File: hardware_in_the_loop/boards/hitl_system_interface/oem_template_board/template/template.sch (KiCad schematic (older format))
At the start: 39 parts, among them J1 CONN_02X03, U1 MCP2561-E_SN, U101 TPS560430YF, U2 ATMEGA16M1, Y1 Crystal_SMD

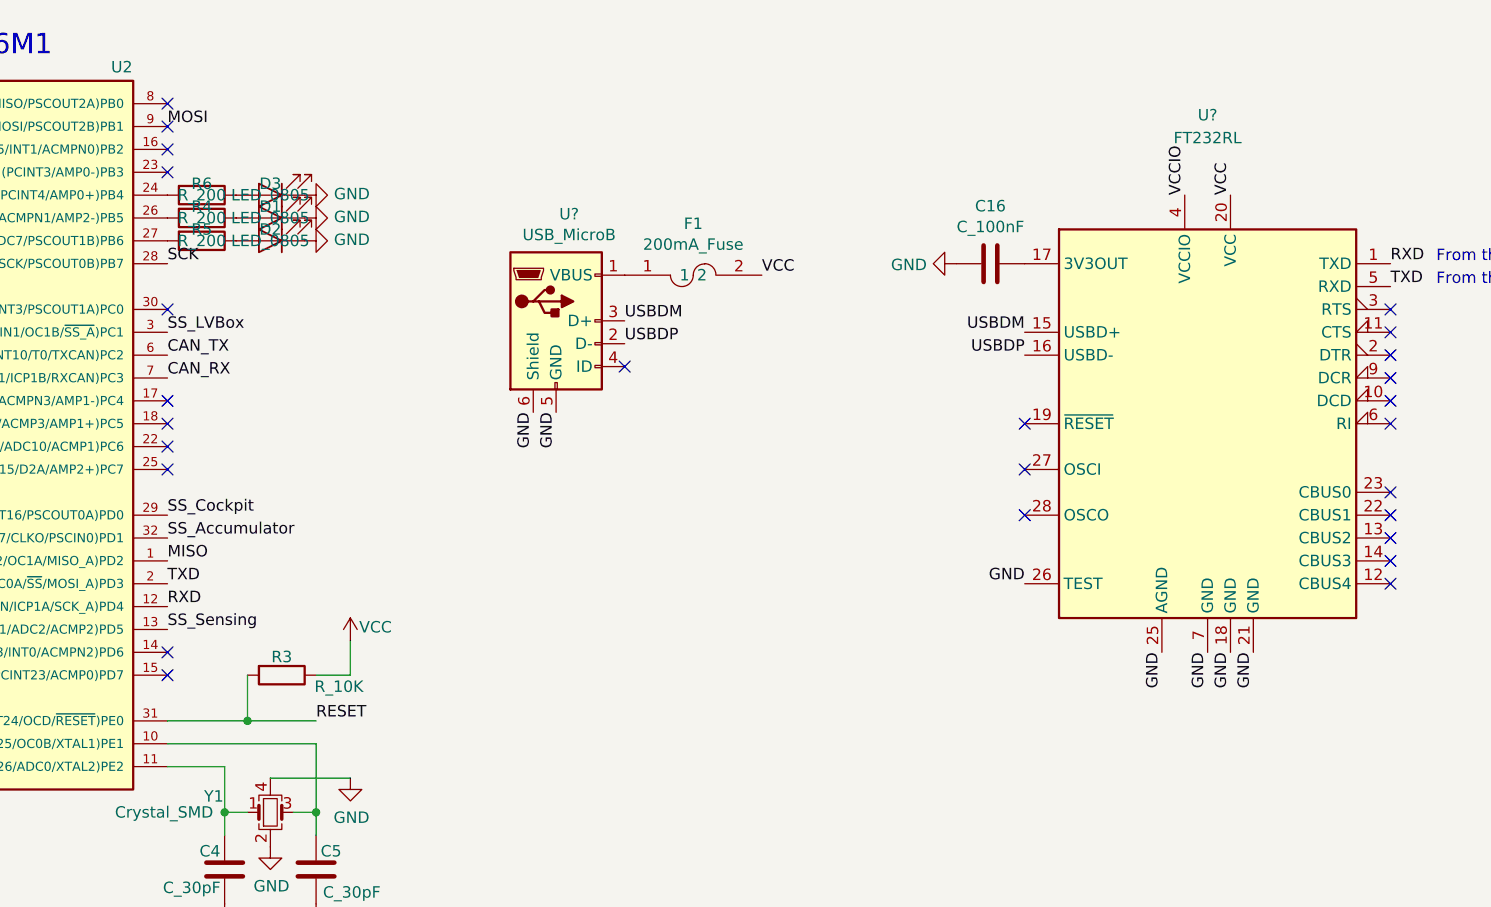
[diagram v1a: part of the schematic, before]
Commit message: Changed GND and VCC pins to power flags, added Nanofit8 connector, modified USBDP and USBDM connections on USB_Micro and FT232RL
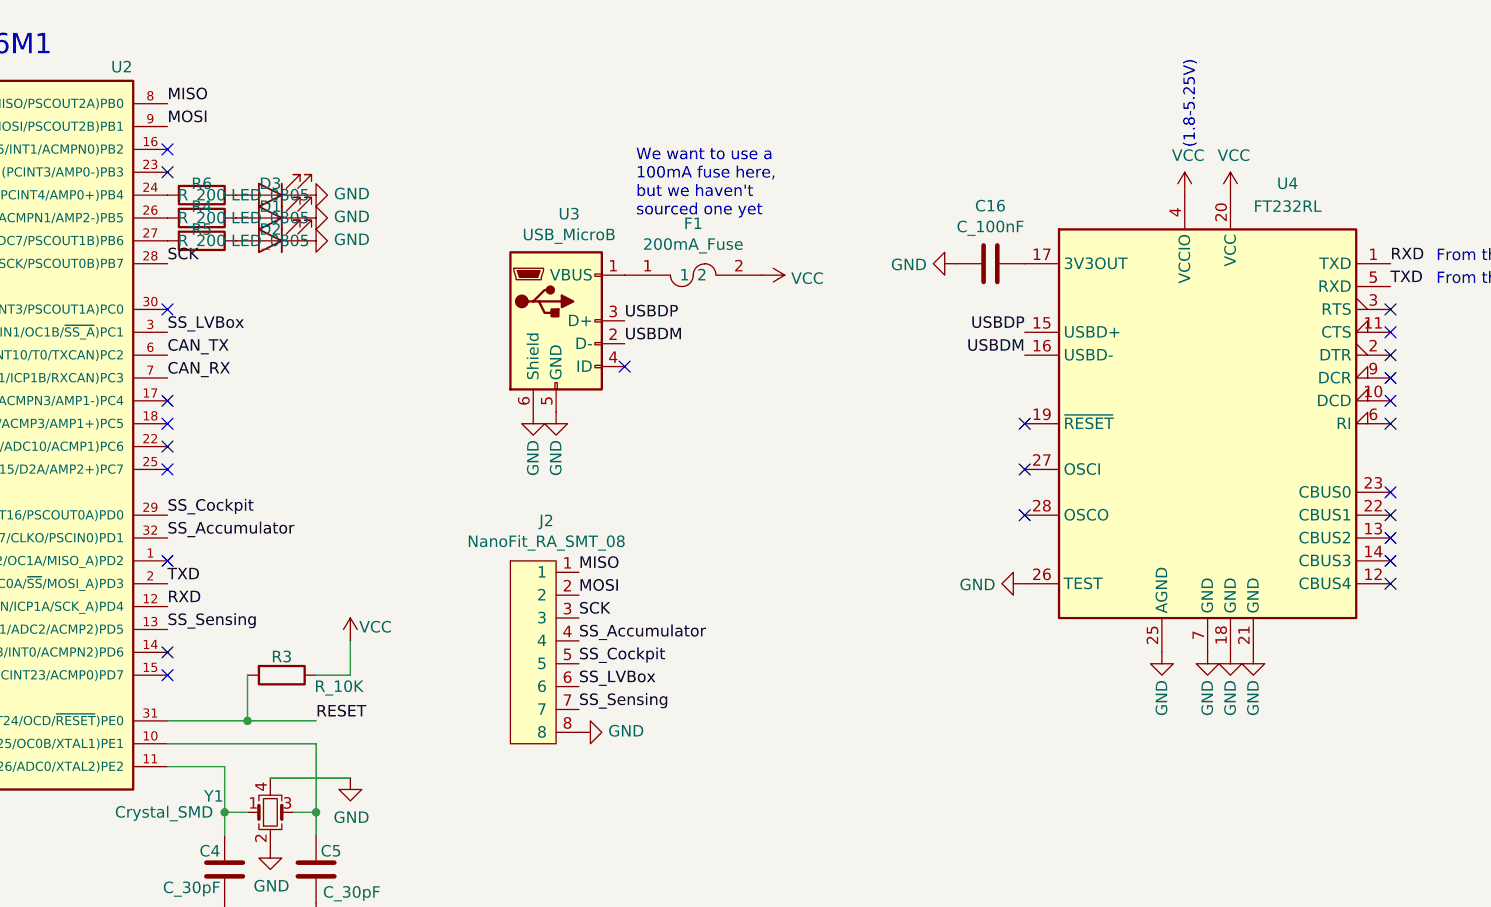
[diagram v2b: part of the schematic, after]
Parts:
- added J2: NanoFit_RA_SMT_08, footprints:NanoFit_RA_8, symbol formula:NanoFit_RA_SMT_08
- gave numbers to parts that had none: 2
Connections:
- net VCCIO is gone; now on net VCC: U4.4 (VCCIO)
- net GND: now also J2.8
- net MISO: now also U2.8 ((PCINT0/MISO/PSCOUT2A)PB0), J2.1; no longer U2.1 ((PCINT18/PSCIN2/OC1A/MISO_A)PD2)
- net MOSI: now also J2.2
- net SCK: now also J2.3
- net SS_Accumulator: now also J2.4
- net SS_Cockpit: now also J2.5
- net SS_LVBox: now also J2.6
- net SS_Sensing: now also J2.7
- net USBDM: now also U3.2 (D-), U4.16 (USBD-); no longer U3.3 (D+), U4.15 (USBD+)
- net USBDP: now also U3.3 (D+), U4.15 (USBD+); no longer U3.2 (D-), U4.16 (USBD-)
- no-connect marks 28 -> 27
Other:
- note added: "(1.8-5.25V)"
- note added: "We want to use a \n100mA fuse here, \nbut we haven't \nsourced one yet\n"
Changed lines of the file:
@@
 Text Label 3650 2200 0    50   ~ 0
 CAN_RX
-Text Label 3650 3000 0    50   ~ 0
-MISO
 Text Label 3650 1100 0    50   ~ 0
 MOSI
@@
 	0    -1   -1   0
 $EndComp
-NoConn ~ 3650 1000
-NoConn ~ 3650 1100
 NoConn ~ 3650 1200
 NoConn ~ 3650 1300
@@
 NoConn ~ 9000 1900
 NoConn ~ 9000 2000
-Text Label 8000 3400 3    50   ~ 0
-GND
-Text Label 8200 3400 3    50   ~ 0
-GND
-Text Label 8300 3400 3    50   ~ 0
-GND
-Text Label 8400 3400 3    50   ~ 0
-GND
-Text Label 7400 3100 2    50   ~ 0
-GND
 NoConn ~ 9000 2700
 NoConn ~ 9000 2800
@@
 $EndComp
 $Comp
-L power:GND #PWR?
+L power:GND #PWR028
 U 1 1 5FA19E14
 P 7100 1700
-F 0 "#PWR?" H 7100 1450 50  0001 C CNN
+F 0 "#PWR028" H 7100 1450 50  0001 C CNN
 F 1 "GND" V 7105 1572 50  0000 R CNN
 F 2 "" H 7100 1700 50  0001 C CNN
@@
 $EndComp
 $Comp
-L formula:USB_MicroB U?
+L formula:USB_MicroB U3
 U 1 1 5FA24431
 P 5350 1950
-F 0 "U?" H 5407 2417 50  0000 C CNN
+F 0 "U3" H 5407 2417 50  0000 C CNN
 F 1 "USB_MicroB" H 5407 2326 50  0000 C CNN
 F 2 "Connectors_USB:USB_Micro-B_Molex-105017-0001" H 5300 2300 50  0001 C CNN
@@
 	1    0    0    -1
 $EndComp
-Text Label 5350 2350 3    50   ~ 0
-GND
-Text Label 5250 2350 3    50   ~ 0
-GND
 NoConn ~ 5650 2150
 $Comp
-L formula:FT232RL U?
+L formula:FT232RL U4
 U 1 1 5F9FAF59
 P 8200 2400
-F 0 "U?" H 8200 3750 50  0000 C CNN
-F 1 "FT232RL" H 8200 3650 50  0000 C CNN
+F 0 "U4" H 8550 3450 50  0000 C CNN
+F 1 "FT232RL" H 8550 3350 50  0000 C CNN
 F 2 "Package_SO:SSOP-28_5.3x10.2mm_P0.65mm" H 9300 1500 50  0001 C CNN
 F 3 "https://www.ftdichip.com/Support/Documents/DataSheets/ICs/DS_FT232R.pdf" H 8200 2400 50  0001 C CNN
@@
 	1    0    0    -1
 $EndComp
-Text Label 8300 1400 1    50   ~ 0
-VCC
 Text Label 7400 2000 2    50   ~ 0
+USBDP
+Text Label 7400 2100 2    50   ~ 0
 USBDM
-Text Label 7400 2100 2    50   ~ 0
+Text Label 5650 1950 0    50   ~ 0
 USBDP
-Text Label 8100 1400 1    50   ~ 0
-VCCIO
-Text Label 5650 1950 0    50   ~ 0
+Text Label 5650 2050 0    50   ~ 0
 USBDM
-Text Label 5650 2050 0    50   ~ 0
-USBDP
 NoConn ~ 7400 2400
 NoConn ~ 7400 2600
@@
 	1    0    0    -1
 $EndComp
-Text Label 6250 1750 0    50   ~ 0
-VCC
+Text Label 3650 1000 0    50   ~ 0
+MISO
+NoConn ~ 3650 3000
+Text Notes 5700 1500 0    50   ~ 0
+We want to use a \n100mA fuse here, \nbut we haven't \nsourced one yet\n
+$Comp
+L power:GND #PWR025
+U 1 1 5FA26E89
+P 5350 2350
+F 0 "#PWR025" H 5350 2100 50  0001 C CNN
+F 1 "GND" V 5350 2150 50  0000 C CNN
+F 2 "" H 5350 2350 50  0001 C CNN
+F 3 "" H 5350 2350 50  0001 C CNN
+	1    5350 2350
+	1    0    0    -1
+$EndComp
+$Comp
+L power:GND #PWR024
+U 1 1 5FA2D38B
+P 5250 2350
+F 0 "#PWR024" H 5250 2100 50  0001 C CNN
+F 1 "GND" V 5250 2150 50  0000 C CNN
+F 2 "" H 5250 2350 50  0001 C CNN
+F 3 "" H 5250 2350 50  0001 C CNN
+	1    5250 2350
+	1    0    0    -1
+$EndComp
+$Comp
+L power:VCC #PWR027
+U 1 1 5FA2F0E9
+P 6250 1750
+F 0 "#PWR027" H 6250 1600 50  0001 C CNN
+F 1 "VCC" V 6265 1878 50  0000 L CNN
+F 2 "" H 6250 1750 50  0001 C CNN
+F 3 "" H 6250 1750 50  0001 C CNN
+	1    6250 1750
+	0    1    1    0
+$EndComp
+$Comp
+L power:VCC #PWR033
+U 1 1 5FA315C6
+P 8300 1400
+F 0 "#PWR033" H 8300 1250 50  0001 C CNN
+F 1 "VCC" H 8315 1573 50  0000 C CNN
+F 2 "" H 8300 1400 50  0001 C CNN
+F 3 "" H 8300 1400 50  0001 C CNN
+	1    8300 1400
+	1    0    0    -1
+$EndComp
+$Comp
+L power:VCC #PWR031
+U 1 1 5FA321E6
+P 8100 1400
+F 0 "#PWR031" H 8100 1250 50  0001 C CNN
+F 1 "VCC" H 8115 1573 50  0000 C CNN
+F 2 "" H 8100 1400 50  0001 C CNN
+F 3 "" H 8100 1400 50  0001 C CNN
+	1    8100 1400
+	1    0    0    -1
+$EndComp
+Text Notes 8150 1200 1    50   ~ 0
+(1.8-5.25V)
+$Comp
+L power:GND #PWR030
+U 1 1 5FA36AB2
+P 8000 3400
+F 0 "#PWR030" H 8000 3150 50  0001 C CNN
+F 1 "GND" V 8000 3200 50  0000 C CNN
+F 2 "" H 8000 3400 50  0001 C CNN
+F 3 "" H 8000 3400 50  0001 C CNN
+	1    8000 3400
+	1    0    0    -1
+$EndComp
+$Comp
+L power:GND #PWR032
+U 1 1 5FA373FB
+P 8200 3400
+F 0 "#PWR032" H 8200 3150 50  0001 C CNN
+F 1 "GND" V 8200 3200 50  0000 C CNN
+F 2 "" H 8200 3400 50  0001 C CNN
+F 3 "" H 8200 3400 50  0001 C CNN
+	1    8200 3400
+	1    0    0    -1
+$EndComp
+$Comp
+L power:GND #PWR034
+U 1 1 5FA37A7B
+P 8300 3400
+F 0 "#PWR034" H 8300 3150 50  0001 C CNN
+F 1 "GND" V 8300 3200 50  0000 C CNN
+F 2 "" H 8300 3400 50  0001 C CNN
+F 3 "" H 8300 3400 50  0001 C CNN
+	1    8300 3400
+	1    0    0    -1
+$EndComp
+$Comp
+L power:GND #PWR035
+U 1 1 5FA38001
+P 8400 3400
+F 0 "#PWR035" H 8400 3150 50  0001 C CNN
+F 1 "GND" V 8400 3200 50  0000 C CNN
+F 2 "" H 8400 3400 50  0001 C CNN
+F 3 "" H 8400 3400 50  0001 C CNN
+	1    8400 3400
+	1    0    0    -1
+$EndComp
+$Comp
+L power:GND #PWR029
+U 1 1 5FA39AB7
+P 7400 3100
+F 0 "#PWR029" H 7400 2850 50  0001 C CNN
+F 1 "GND" V 7405 2972 50  0000 R CNN
+F 2 "" H 7400 3100 50  0001 C CNN
+F 3 "" H 7400 3100 50  0001 C CNN
+	1    7400 3100
+	0    1    1    0
+$EndComp
+$Comp
+L formula:NanoFit_RA_SMT_08 J2
+U 1 1 5FA3D7DF
+P 5250 3200
+F 0 "J2" H 5308 3575 50  0000 C CNN
+F 1 "NanoFit_RA_SMT_08" H 5308 3484 50  0000 C CNN
+F 2 "footprints:NanoFit_RA_8" H 4950 2550 50  0001 C CNN
+F 3 "" H 5250 3450 50  0001 C CNN
+	1    5250 3200
+	1    0    0    -1
+$EndComp
+Text Label 5450 3050 0    50   ~ 0
+MISO
+Text Label 5450 3150 0    50   ~ 0
+MOSI
+Text Label 5450 3250 0    50   ~ 0
+SCK
+Text Label 5450 3350 0    50   ~ 0
+SS_Accumulator
+Text Label 5450 3450 0    50   ~ 0
+SS_Cockpit
+Text Label 5450 3550 0    50   ~ 0
+SS_LVBox
+Text Label 5450 3650 0    50   ~ 0
+SS_Sensing
+$Comp
+L power:GND #PWR026
+U 1 1 5FA45E26
+P 5450 3750
+F 0 "#PWR026" H 5450 3500 50  0001 C CNN
+F 1 "GND" V 5455 3622 50  0000 R CNN
+F 2 "" H 5450 3750 50  0001 C CNN
+F 3 "" H 5450 3750 50  0001 C CNN
+	1    5450 3750
+	0    -1   -1   0
+$EndComp
 $EndSCHEMATC
